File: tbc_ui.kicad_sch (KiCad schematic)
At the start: 39 parts, among them J1 75869-105LF, SW1 PEC11R-4220F-S0024, SW2 TL1100F160Q, U1 CD74HC14M96, U2 ICM7555CBAZ

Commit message: initial board layout
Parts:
- C1, C2, C3: footprint (none) -> tbc-ui:C0603; symbol tbc:GCM188R71H103KA37J -> tbc-ui:GCM188R71H103KA37J
- C4: footprint (none) -> tbc-ui:C0603; symbol tbc:GCJ188R71E105KA01D -> tbc-ui:GCJ188R71E105KA01D
- C5, C6, C7: footprint (none) -> tbc-ui:C0603; symbol tbc:GCJ188R71H104KA12D -> tbc-ui:GCJ188R71H104KA12D
- D1, D2, D3: footprint (none) -> tbc-ui:1N4148WS; symbol tbc:1N4148WS -> tbc-ui:1N4148WS
- D10: symbol tbc:WP424NDT -> tbc-ui:WP424NDT
- D4: symbol tbc:WP424IDT -> tbc-ui:WP424IDT
- D5, D6, D7, D8, D9: symbol tbc:WP424GDT -> tbc-ui:WP424GDT
- DS1: footprint (none) -> tbc-ui:NHD-0420CW; symbol tbc:NHD-0420CW-AW3 -> tbc-ui:NHD-0420CW-AW3
- J1: footprint (none) -> tbc-ui:75869-105LF; symbol tbc:75869-105LF -> tbc-ui:75869-105LF
- R1, R2, R3, R4, R5, R6, R8, R9: footprint (none) -> tbc-ui:R0603; symbol tbc:RC0603FR-0710KL -> tbc-ui:RC0603FR-0710KL
- R10, R11, R12, R13, R14, R15, R16: footprint (none) -> tbc-ui:R0603; symbol tbc:RC0603FR-07560RL -> tbc-ui:RC0603FR-07560RL
- R7: footprint (none) -> tbc-ui:R0603; symbol tbc:RC0603FR-07100KL -> tbc-ui:RC0603FR-07100KL
- SW1: footprint (none) -> tbc-ui:PEC11R-4xxxF-Sxxx; symbol tbc:PEC11R-4220F-S0024 -> tbc-ui:PEC11R-4220F-S0024
- SW2: symbol tbc:TL1100F160Q -> tbc-ui:TL1100F160Q
- U1: footprint (none) -> tbc-ui:SOIC-14; symbol tbc:CD74HC14M96 -> tbc-ui:CD74HC14M96
- U2: symbol tbc:ICM7555CBAZ -> tbc-ui:ICM7555CBAZ; Mouser 968-ICM7555CBAZ -> 968-ICM7555CBAZ

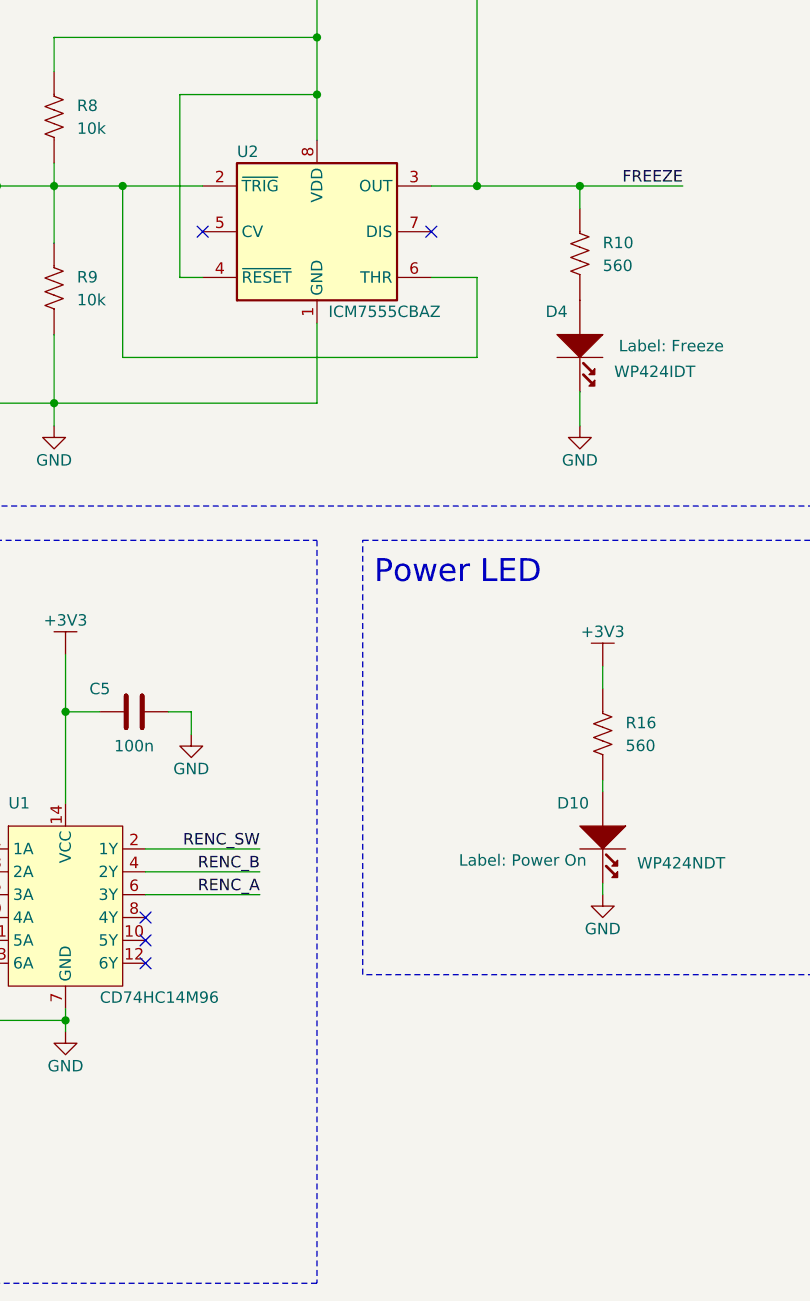
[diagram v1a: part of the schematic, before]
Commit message: additional footprints and layout
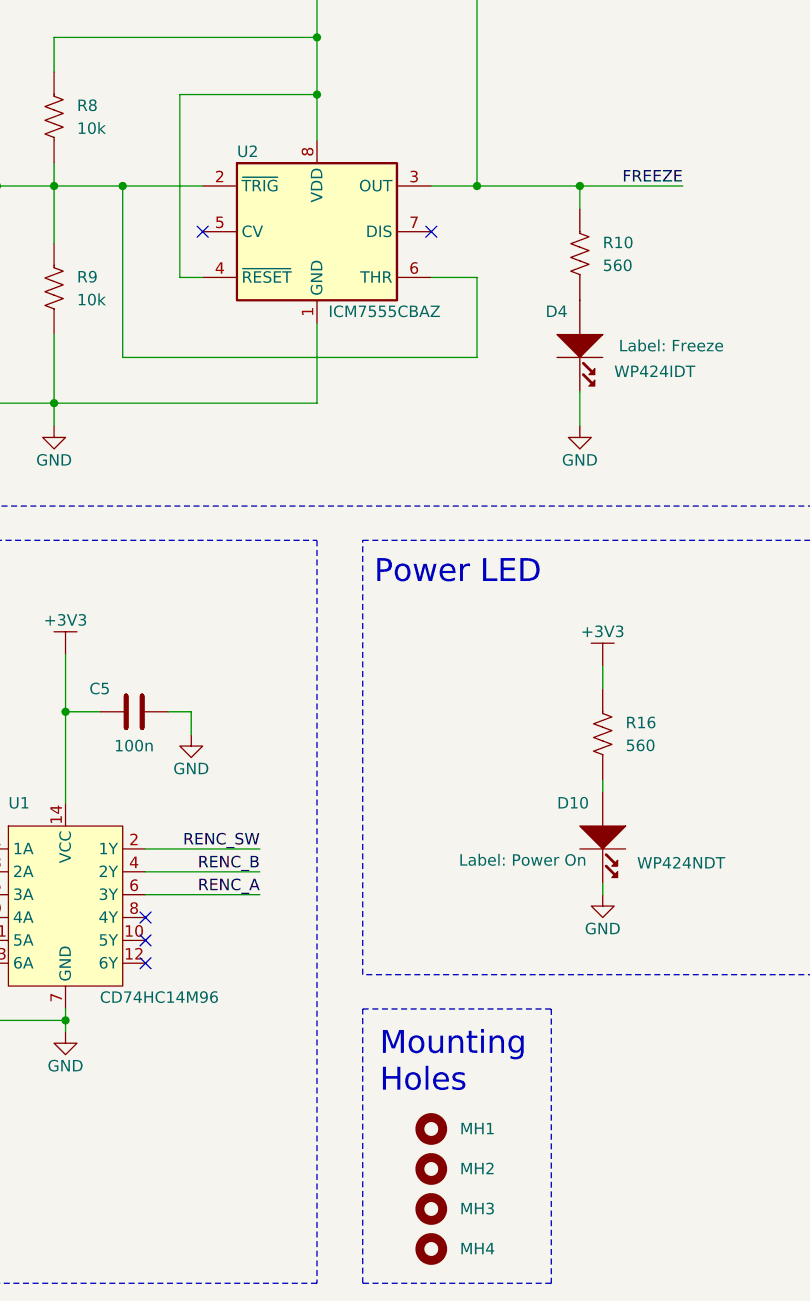
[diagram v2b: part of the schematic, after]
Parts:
- added MH1, MH2, MH3, MH4: MH_7.4MMNCx3.2MMD, tbc-ui:MH_7.4MMCx3.2MMD_NON_COPPER_NPTH, symbol tbc-ui:MH_7.4MMNCx3.2MMD
- D10, D4, D5, D6, D7, D8, D9: footprint (none) -> tbc-ui:WP424
- U2: footprint (none) -> tbc-ui:SOIC-8
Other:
- note added: "Mounting Holes"
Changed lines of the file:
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@@
     (stroke (width 0) (type default))
+  )
+  (rectangle (start 152.4 162.56) (end 173.355 193.04)
+    (stroke (width 0) (type dash))
+    (fill (type none))
   )
   (rectangle (start 17.78 16.51) (end 71.12 106.68)
@@
     (stroke (width 0) (type dash))
     (fill (type none))
+  )
+  (text "Mounting\nHoles" (at 154.305 172.085 0)
+    (effects (font (size 2.54 2.54)) (justify left bottom))
   )
   (text "Connector" (at 19.05 21.59 0)
@@
       (effects (font (size 1.27 1.27)) (justify left))
     )
-    (property "Footprint" "" (at 165.1 90.17 0)
+    (property "Footprint" "tbc-ui:WP424" (at 165.1 90.17 0)
       (effects (font (size 1.27 1.27)) hide)
     )
@@
       (effects (font (size 1.27 1.27)))
     )
-    (property "Footprint" "" (at 220.98 142.24 0)
+    (property "Footprint" "tbc-ui:WP424" (at 220.98 142.24 0)
       (effects (font (size 1.27 1.27)) hide)
     )
@@
     )
   )
+  (symbol (lib_id "tbc-ui:MH_7.4MMNCx3.2MMD") (at 160.02 184.785 0) (unit 1)
+    (in_bom no) (on_board yes) (dnp no) (fields_autoplaced)
+    (property "Reference" "MH3" (at 163.195 184.785 0)
+      (effects (font (size 1.27 1.27)) (justify left))
+    )
+    (property "Value" "MH_7.4MMNCx3.2MMD" (at 161.29 192.405 0)
+      (effects (font (size 1.27 1.27)) hide)
+    )
+    (property "Footprint" "tbc-ui:MH_7.4MMCx3.2MMD_NON_COPPER_NPTH" (at 160.02 194.945 0) (show_name)
+      (effects (font (size 1.27 1.27)) hide)
+    )
+    (property "Datasheet" "" (at 160.02 182.245 0)
+      (effects (font (size 1.27 1.27)) hide)
+    )
+    (property "Sim.Enable" "0" (at 160.02 188.595 0) (show_name)
+      (effects (font (size 1.27 1.27)) hide)
+    )
+    (instances
+      (project "tbc_ui"
+        (path "/25cb95a4-db47-42c7-9003-b39117adea44"
+          (reference "MH3") (unit 1)
+        )
+      )
+    )
+  )
   (symbol (lib_id "tbc-ui:WP424NDT") (at 179.07 144.78 270) (unit 1)
     (in_bom yes) (on_board yes) (dnp no)
@@
       (effects (font (size 1.27 1.27)) (justify left))
     )
-    (property "Footprint" "" (at 167.64 144.78 0)
+    (property "Footprint" "tbc-ui:WP424" (at 167.64 144.78 0)
       (effects (font (size 1.27 1.27)) hide)
     )
@@
     )
   )
+  (symbol (lib_id "tbc-ui:MH_7.4MMNCx3.2MMD") (at 160.02 189.23 0) (unit 1)
+    (in_bom no) (on_board yes) (dnp no) (fields_autoplaced)
+    (property "Reference" "MH4" (at 163.195 189.23 0)
+      (effects (font (size 1.27 1.27)) (justify left))
+    )
+    (property "Value" "MH_7.4MMNCx3.2MMD" (at 161.29 196.85 0)
+      (effects (font (size 1.27 1.27)) hide)
+    )
+    (property "Footprint" "tbc-ui:MH_7.4MMCx3.2MMD_NON_COPPER_NPTH" (at 160.02 199.39 0) (show_name)
+      (effects (font (size 1.27 1.27)) hide)
+    )
+    (property "Datasheet" "" (at 160.02 186.69 0)
+      (effects (font (size 1.27 1.27)) hide)
+    )
+    (property "Sim.Enable" "0" (at 160.02 193.04 0) (show_name)
+      (effects (font (size 1.27 1.27)) hide)
+    )
+    (instances
+      (project "tbc_ui"
+        (path "/25cb95a4-db47-42c7-9003-b39117adea44"
+          (reference "MH4") (unit 1)
+        )
+      )
+    )
+  )
   (symbol (lib_id "tbc-ui:PWR_FLAG") (at 46.99 33.02 0) (unit 1)
     (in_bom yes) (on_board yes) (dnp no)
@@
       (effects (font (size 1.27 1.27)))
     )
-    (property "Footprint" "" (at 243.84 142.24 0)
+    (property "Footprint" "tbc-ui:WP424" (at 243.84 142.24 0)
       (effects (font (size 1.27 1.27)) hide)
     )
@@
       (effects (font (size 1.27 1.27)))
     )
-    (property "Footprint" "" (at 255.27 142.24 0)
+    (property "Footprint" "tbc-ui:WP424" (at 255.27 142.24 0)
       (effects (font (size 1.27 1.27)) hide)
     )
@@
     )
   )
+  (symbol (lib_id "tbc-ui:MH_7.4MMNCx3.2MMD") (at 160.02 175.895 0) (unit 1)
+    (in_bom no) (on_board yes) (dnp no) (fields_autoplaced)
+    (property "Reference" "MH1" (at 163.195 175.895 0)
+      (effects (font (size 1.27 1.27)) (justify left))
+    )
+    (property "Value" "MH_7.4MMNCx3.2MMD" (at 161.29 183.515 0)
+      (effects (font (size 1.27 1.27)) hide)
+    )
+    (property "Footprint" "tbc-ui:MH_7.4MMCx3.2MMD_NON_COPPER_NPTH" (at 160.02 186.055 0) (show_name)
+      (effects (font (size 1.27 1.27)) hide)
+    )
+    (property "Datasheet" "" (at 160.02 173.355 0)
+      (effects (font (size 1.27 1.27)) hide)
+    )
+    (property "Sim.Enable" "0" (at 160.02 179.705 0) (show_name)
+      (effects (font (size 1.27 1.27)) hide)
+    )
+    (instances
+      (project "tbc_ui"
+        (path "/25cb95a4-db47-42c7-9003-b39117adea44"
+          (reference "MH1") (unit 1)
+        )
+      )
+    )
+  )
   (symbol (lib_id "tbc-ui:RC0603FR-07560RL") (at 179.07 132.08 90) (unit 1)
     (in_bom yes) (on_board yes) (dnp no) (fields_autoplaced)
@@
       (effects (font (size 1.27 1.27)))
     )
-    (property "Footprint" "" (at 209.55 142.24 0)
+    (property "Footprint" "tbc-ui:WP424" (at 209.55 142.24 0)
       (effects (font (size 1.27 1.27)) hide)
     )
@@
         (path "/25cb95a4-db47-42c7-9003-b39117adea44"
           (reference "C3") (unit 1)
+        )
+      )
+    )
+  )
+  (symbol (lib_id "tbc-ui:MH_7.4MMNCx3.2MMD") (at 160.02 180.34 0) (unit 1)
+    (in_bom no) (on_board yes) (dnp no) (fields_autoplaced)
+    (property "Reference" "MH2" (at 163.195 180.34 0)
+      (effects (font (size 1.27 1.27)) (justify left))
+    )
+    (property "Value" "MH_7.4MMNCx3.2MMD" (at 161.29 187.96 0)
+      (effects (font (size 1.27 1.27)) hide)
+    )
+    (property "Footprint" "tbc-ui:MH_7.4MMCx3.2MMD_NON_COPPER_NPTH" (at 160.02 190.5 0) (show_name)
+      (effects (font (size 1.27 1.27)) hide)
+    )
+    (property "Datasheet" "" (at 160.02 177.8 0)
+      (effects (font (size 1.27 1.27)) hide)
+    )
+    (property "Sim.Enable" "0" (at 160.02 184.15 0) (show_name)
+      (effects (font (size 1.27 1.27)) hide)
+    )
+    (instances
+      (project "tbc_ui"
+        (path "/25cb95a4-db47-42c7-9003-b39117adea44"
+          (reference "MH2") (unit 1)
         )
       )
@@
       (effects (font (size 1.27 1.27)) (justify left))
     )
-    (property "Footprint" "" (at 163.83 86.36 0)
+    (property "Footprint" "tbc-ui:SOIC-8" (at 163.83 86.36 0)
       (effects (font (size 1.27 1.27)) hide)
     )
@@
       (effects (font (size 1.27 1.27)))
     )
-    (property "Footprint" "" (at 232.41 142.24 0)
-      (effects (font (size 1.27 1.27)) hide)
-    )
+    (property "Footprint" "tbc-ui:WP424" (at 232.41 142.24 0)
+      (effects (font (size 1.27 1.27)) hide)
+    )

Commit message: updated to Kicad 8, finished footprints and layouts, erc passed
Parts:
- SW2: footprint (none) -> tbc-ui:TL1100F
